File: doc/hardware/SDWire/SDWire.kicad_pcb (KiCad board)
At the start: 2 copper layers, 21.6 x 48.4 mm, 82 parts, among them J1 usd-plug, J2 uSD Socket, P1 USB_OTG_MICRO_USB, Q3 MMBT4403LT1, Q4 MMBT4403LT1, U1 USB2640-HZH-02, U2 SPX3819M5, U3 FT200XD, U4 MC74HC1G04DTT1G, U5 TS3A27518EPWR, Y1 24MHz

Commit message: Fix silkscreen and fabrication layers
Change-Id: Ifa4360e38b6398d27db0764db9cf22207d5504e1
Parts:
- U1: footprint Housings_DFN_QFN:QFN-48-1EP_7x7mm_Pitch0.5mm -> mux-footprints:QFN-48-1EP_7x7mm_Pitch0.5mm
- U3: footprint Housings_DFN_QFN:DFN-10-1EP_3x3mm_Pitch0.5mm -> mux-footprints:DFN-10-1EP_3x3mm_Pitch0.5mm
- Y1: footprint Crystals:Crystal_SMD_2520-4pin_2.5x2.0mm -> mux-footprints:Crystal_SMD_2520-4pin_2.5x2.0mm

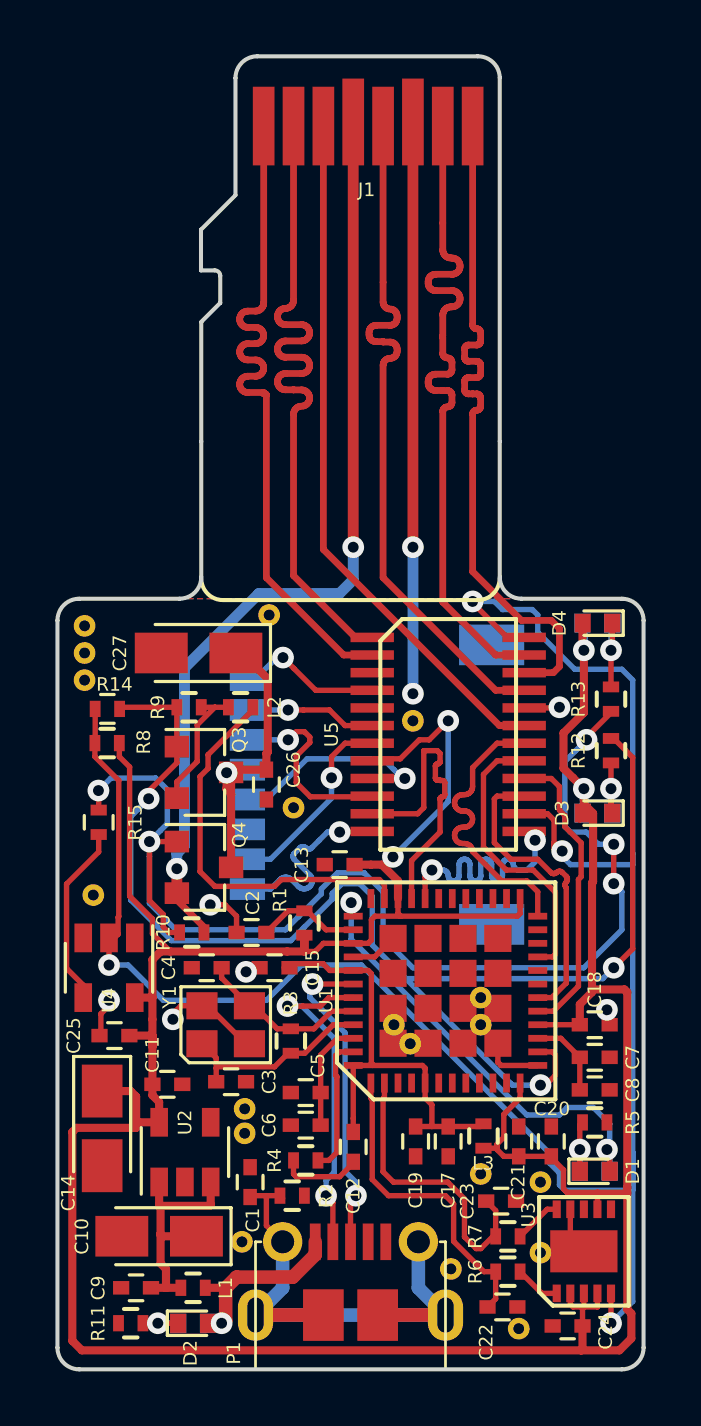
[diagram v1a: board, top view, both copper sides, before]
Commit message: Fix LEDs and card detect connections
Change-Id: I041ff52d267cebffd98fdaa6a1c2b5b6e2d7bece
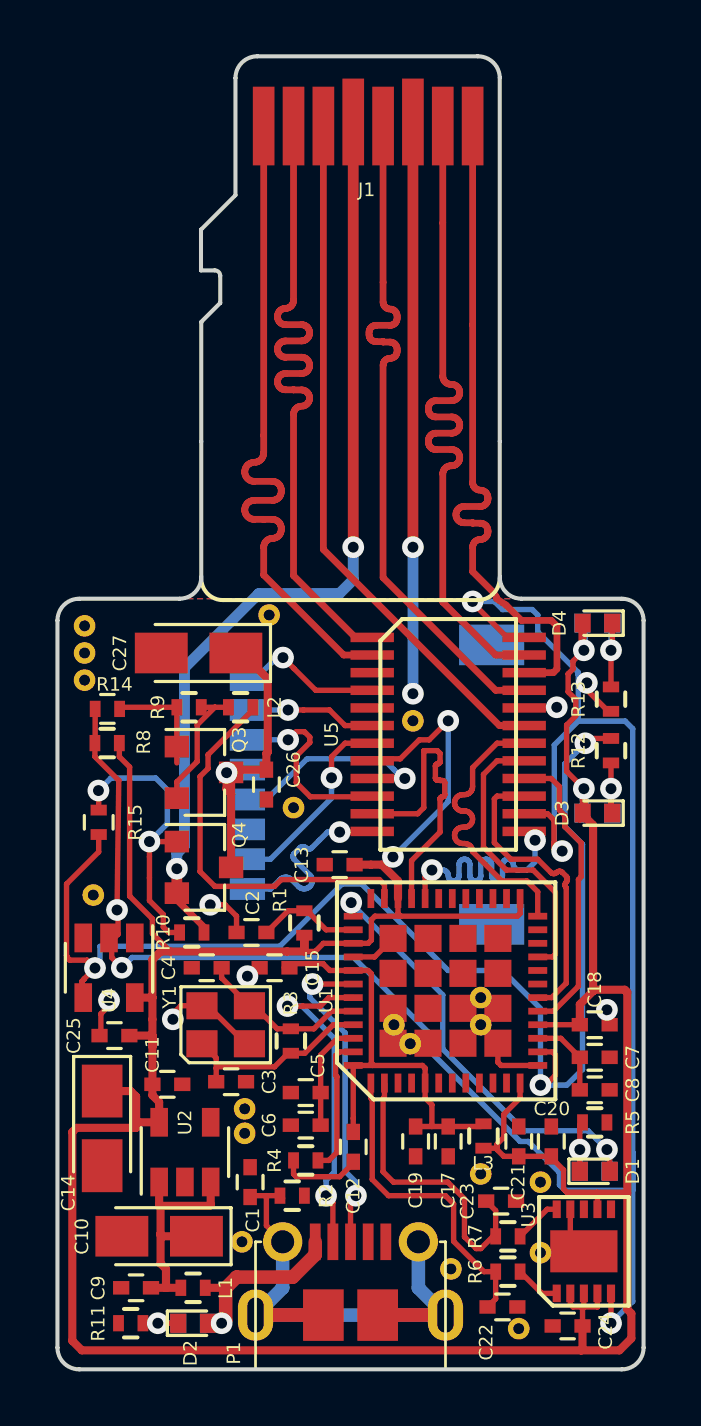
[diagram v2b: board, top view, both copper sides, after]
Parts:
- R8: value 10K -> DNP
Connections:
- Q3 pad 1: /~CD_TS -> Net-(Q3-Pad1)
- R13 pad 2: Net-(Q4-Pad1) -> /SOCKET_SEL
- R14 pad 1: /~CD_TS -> Net-(Q3-Pad1)
- R15 pad 2: Net-(R15-Pad2) -> /~CD_TS
- R9 pad 1: /~CD_TS -> Net-(Q3-Pad1)
- U4 pad 4: Net-(R15-Pad2) -> /~CD_TS
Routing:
- net Net-(Q4-Pad1): track 45.4 -> 10.9 mm, vias 5 -> 2
- net Net-(R15-Pad2): track 6.76 -> 0.00 mm
- net Net-(Q3-Pad1): track 0.00 -> 4.18 mm
- net /SOCKET_SEL: track 77.3 -> 80.6 mm, vias 4 -> 6
- net /~CD_TS: track 49.9 -> 48.4 mm
- net Net-(D1-Pad2): track 17.9 -> 16.6 mm
